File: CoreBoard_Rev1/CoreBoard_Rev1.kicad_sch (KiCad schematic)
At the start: 86 parts, among them J1 RJ45_LED_Shielded, SW1 SW_Push, SW10 SW_Push, SW11 SW_Push, SW12 SW_Push, SW13 SW_Push, SW14 SW_Push, SW15 SW_Push, SW16 SW_SPDT, SW2 SW_Push, SW3 SW_Push, SW4 SW_Push, SW5 SW_Push, SW6 SW_Push, SW7 SW_Push, SW8 SW_Push, SW9 SW_Push, U1 Teensy4.1_DEV-16771, U2 TSR_1-2450, U4 74HC148, U5 74HC148, U6 74HC00, U7 OKI

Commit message: connected remaining components
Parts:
- U2: footprint Converter_DCDC:Converter_DCDC_TRACO_TSR-1_THT -> MRDT_Devices:SHHD003A0A-SRZ
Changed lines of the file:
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@@
       (effects (font (size 1.27 1.27)))
     )
-    (property "Footprint" "Converter_DCDC:Converter_DCDC_TRACO_TSR-1_THT" (at 124.46 44.45 0)
+    (property "Footprint" "MRDT_Devices:SHHD003A0A-SRZ" (at 124.46 44.45 0)
       (effects (font (size 1.27 1.27) italic) (justify left) hide)
     )

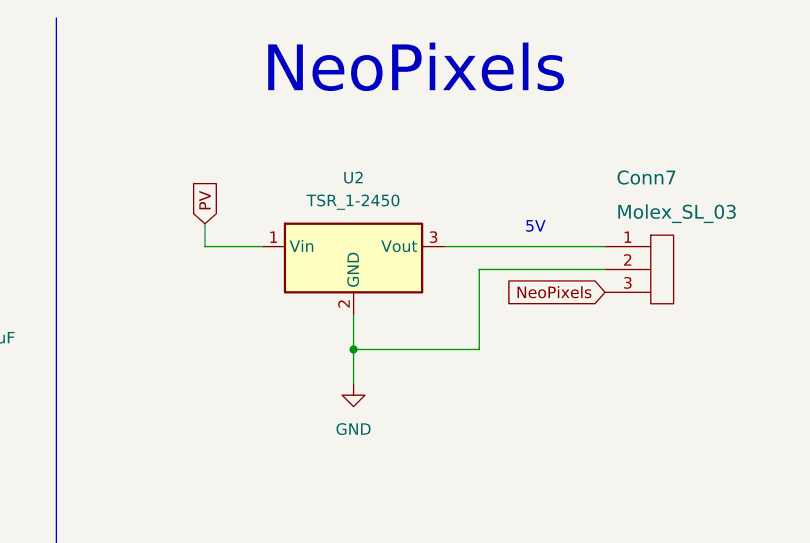
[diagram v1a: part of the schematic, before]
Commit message: updating button traces
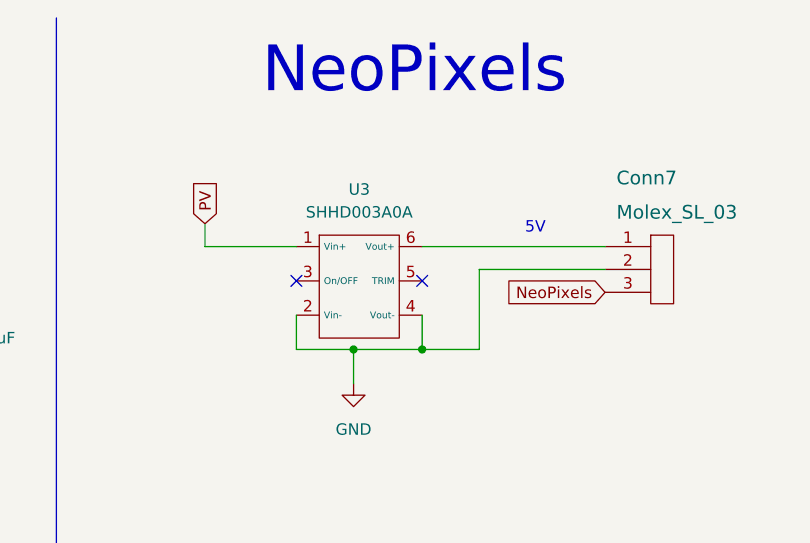
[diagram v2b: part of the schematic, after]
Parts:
- removed U2: TSR_1-2450, MRDT_Devices:SHHD003A0A-SRZ, symbol Regulator_Switching:TSR_1-2450
- added U3: SHHD003A0A, MRDT_Devices:SHHD003A0A-SRZ, symbol MRDT_Devices:SHHD003A0A
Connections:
- net GND: now also U3.2 (Vin-), U3.4 (Vout-)
- net PV: now also U3.1 (Vin+)
- net at Conn7.1: now also U3.6 (Vout+)
- no-connect marks 28 -> 30
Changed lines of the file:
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@@
   (junction (at 308.61 53.34) (diameter 0) (color 0 0 0 0)
   )
+  (junction (at 124.46 49.53) (diameter 0) (color 0 0 0 0)
+  )
   (junction (at 369.57 40.64) (diameter 0) (color 0 0 0 0)
   )
@@
   (junction (at 224.79 111.76) (diameter 0) (color 0 0 0 0)
   )
-  (junction (at 124.46 49.53) (diameter 0) (color 0 0 0 0)
+  (junction (at 132.08 49.53) (diameter 0) (color 0 0 0 0)
   )
   (junction (at 226.06 59.69) (diameter 0) (color 0 0 0 0)
@@
   (no_connect (at 144.78 182.88))
   (no_connect (at 53.34 193.04))
+  (no_connect (at 118.11 41.91))
   (no_connect (at 349.25 152.4))
   (no_connect (at 350.52 201.93))
@@
   (no_connect (at 53.34 223.52))
   (no_connect (at 93.98 256.54))
+  (no_connect (at 132.08 41.91))
   (no_connect (at 93.98 259.08))
   (no_connect (at 53.34 213.36))
@@
     (stroke (width 0) (type default))
   )
+  (wire (pts (xy 132.08 38.1) (xy 152.4 38.1))
+    (stroke (width 0) (type default))
+  )
   (wire (pts (xy 241.3 267.97) (xy 247.65 267.97))
     (stroke (width 0) (type default))
@@
     (stroke (width 0) (type default))
   )
+  (wire (pts (xy 132.08 45.72) (xy 132.08 49.53))
+    (stroke (width 0) (type default))
+  )
   (wire (pts (xy 373.38 144.78) (xy 373.38 179.07))
     (stroke (width 0) (type default))
@@
     (stroke (width 0) (type default))
   )
+  (wire (pts (xy 132.08 49.53) (xy 124.46 49.53))
+    (stroke (width 0) (type default))
+  )
   (wire (pts (xy 212.09 46.99) (xy 215.9 46.99))
     (stroke (width 0) (type default))
@@
     (stroke (width 0) (type default))
   )
-  (wire (pts (xy 107.95 38.1) (xy 114.3 38.1))
+  (wire (pts (xy 107.95 38.1) (xy 118.11 38.1))
     (stroke (width 0) (type default))
   )
@@
     (stroke (width 0) (type default))
   )
-  (wire (pts (xy 134.62 38.1) (xy 152.4 38.1))
-    (stroke (width 0) (type default))
-  )
   (wire (pts (xy 212.09 36.83) (xy 215.9 36.83))
     (stroke (width 0) (type default))
@@
     (stroke (width 0) (type default))
   )
+  (wire (pts (xy 118.11 49.53) (xy 124.46 49.53))
+    (stroke (width 0) (type default))
+  )
   (wire (pts (xy 236.22 49.53) (xy 236.22 59.69))
     (stroke (width 0) (type default))
@@
     (stroke (width 0) (type default))
   )
-  (wire (pts (xy 124.46 45.72) (xy 124.46 49.53))
-    (stroke (width 0) (type default))
-  )
   (wire (pts (xy 224.79 189.23) (xy 232.41 189.23))
     (stroke (width 0) (type default))
@@
     (stroke (width 0) (type default))
   )
+  (wire (pts (xy 118.11 45.72) (xy 118.11 49.53))
+    (stroke (width 0) (type default))
+  )
   (wire (pts (xy 212.09 44.45) (xy 215.9 44.45))
     (stroke (width 0) (type default))
@@
     (stroke (width 0) (type default))
   )
-  (wire (pts (xy 138.43 49.53) (xy 124.46 49.53))
+  (wire (pts (xy 138.43 49.53) (xy 132.08 49.53))
     (stroke (width 0) (type default))
   )
@@
     )
   )
+  (symbol (lib_id "MRDT_Devices:SHHD003A0A") (at 124.46 50.8 0) (unit 1)
+    (in_bom yes) (on_board yes) (dnp no) (fields_autoplaced)
+    (property "Reference" "U3" (at 125.095 31.75 0)
+      (effects (font (size 1.27 1.27)))
+    )
+    (property "Value" "SHHD003A0A" (at 125.095 34.29 0)
+      (effects (font (size 1.27 1.27)))
+    )
+    (property "Footprint" "MRDT_Devices:SHHD003A0A-SRZ" (at 124.46 50.8 0)
+      (effects (font (size 1.27 1.27)) hide)
+    )
+    (property "Datasheet" "https://www.digikey.com/en/products/detail/abb-power-conversion/SHHD003A0A41-SRZ/3993519" (at 124.46 50.8 0)
+      (effects (font (size 1.27 1.27)) hide)
+    )
+    (pin "1")
+    (pin "2")
+    (pin "3")
+    (pin "4")
+    (pin "5")
+    (pin "6")
+    (instances
+      (project "CoreBoard_Rev1"
+        (path "/33647808-cf2c-4b1c-bf2f-58fa6408b099"
+          (reference "U3") (unit 1)
+        )
+      )
+    )
+  )
   (symbol (lib_id "MRDT_Devices:OKI") (at 58.42 43.18 0) (unit 1)
     (in_bom yes) (on_board yes) (dnp no) (fields_autoplaced)
@@
         )
       )
-    )
-  )
-  (symbol (lib_id "Regulator_Switching:TSR_1-2450") (at 124.46 40.64 0) (unit 1)
-    (in_bom yes) (on_board yes) (dnp no) (fields_autoplaced)
-    (property "Reference" "U2" (at 124.46 30.48 0)
-      (effects (font (size 1.27 1.27)))
-    )
-    (property "Value" "TSR_1-2450" (at 124.46 33.02 0)
-      (effects (font (size 1.27 1.27)))
-    )
-    (property "Footprint" "MRDT_Devices:SHHD003A0A-SRZ" (at 124.46 44.45 0)
-      (effects (font (size 1.27 1.27) italic) (justify left) hide)
-    )
-    (property "Datasheet" "http://www.tracopower.com/products/tsr1.pdf" (at 124.46 40.64 0)
-      (effects (font (size 1.27 1.27)) hide)
-    )
-    (pin "1")
-    (pin "2")
-    (pin "3")
-    (instances
-      (project "CoreBoard_Rev1"
-        (path "/33647808-cf2c-4b1c-bf2f-58fa6408b099"
-          (reference "U2") (unit 1)
-        )
-      )

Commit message: Layout Changes
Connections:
- net GND: now also U3.3 (On/OFF)
- no-connect marks 30 -> 29
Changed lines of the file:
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@@
   (junction (at 260.35 147.32) (diameter 0) (color 0 0 0 0)
   )
+  (junction (at 134.62 49.53) (diameter 0) (color 0 0 0 0)
+  )
   (junction (at 283.21 259.08) (diameter 0) (color 0 0 0 0)
   )
@@
   (junction (at 212.09 259.08) (diameter 0) (color 0 0 0 0)
   )
+  (junction (at 115.57 45.72) (diameter 0) (color 0 0 0 0)
+  )
   (junction (at 224.79 111.76) (diameter 0) (color 0 0 0 0)
-  )
-  (junction (at 132.08 49.53) (diameter 0) (color 0 0 0 0)
   )
   (junction (at 226.06 59.69) (diameter 0) (color 0 0 0 0)
@@
   (no_connect (at 93.98 200.66))
   (no_connect (at 144.78 182.88))
+  (no_connect (at 132.08 41.91))
   (no_connect (at 53.34 193.04))
-  (no_connect (at 118.11 41.91))
   (no_connect (at 349.25 152.4))
   (no_connect (at 350.52 201.93))
@@
   (no_connect (at 53.34 223.52))
   (no_connect (at 93.98 256.54))
-  (no_connect (at 132.08 41.91))
   (no_connect (at 93.98 259.08))
   (no_connect (at 53.34 213.36))
@@
     (stroke (width 0) (type default))
   )
+  (wire (pts (xy 115.57 45.72) (xy 118.11 45.72))
+    (stroke (width 0) (type default))
+  )
   (wire (pts (xy 132.08 38.1) (xy 152.4 38.1))
     (stroke (width 0) (type default))
@@
     (stroke (width 0) (type default))
   )
-  (wire (pts (xy 132.08 45.72) (xy 132.08 49.53))
+  (wire (pts (xy 134.62 45.72) (xy 134.62 49.53))
     (stroke (width 0) (type default))
   )
@@
     (stroke (width 0) (type default))
   )
-  (wire (pts (xy 132.08 49.53) (xy 124.46 49.53))
+  (wire (pts (xy 124.46 49.53) (xy 134.62 49.53))
     (stroke (width 0) (type default))
   )
@@
     (stroke (width 0) (type default))
   )
+  (wire (pts (xy 115.57 41.91) (xy 115.57 45.72))
+    (stroke (width 0) (type default))
+  )
   (wire (pts (xy 281.94 181.61) (xy 283.21 181.61))
     (stroke (width 0) (type default))
@@
     (stroke (width 0) (type default))
   )
+  (wire (pts (xy 134.62 45.72) (xy 132.08 45.72))
+    (stroke (width 0) (type default))
+  )
   (wire (pts (xy 224.79 111.76) (xy 224.79 119.38))
     (stroke (width 0) (type default))
@@
     (stroke (width 0) (type default))
   )
+  (wire (pts (xy 118.11 41.91) (xy 115.57 41.91))
+    (stroke (width 0) (type default))
+  )
   (wire (pts (xy 260.35 259.08) (xy 267.97 259.08))
     (stroke (width 0) (type default))
@@
     (stroke (width 0) (type default))
   )
-  (wire (pts (xy 118.11 49.53) (xy 124.46 49.53))
+  (wire (pts (xy 115.57 49.53) (xy 124.46 49.53))
     (stroke (width 0) (type default))
   )
@@
     (stroke (width 0) (type default))
   )
-  (wire (pts (xy 118.11 45.72) (xy 118.11 49.53))
+  (wire (pts (xy 115.57 45.72) (xy 115.57 49.53))
     (stroke (width 0) (type default))
   )
@@
     (stroke (width 0) (type default))
   )
-  (wire (pts (xy 138.43 49.53) (xy 132.08 49.53))
-    (stroke (width 0) (type default))
-  )
+  (wire (pts (xy 138.43 49.53) (xy 134.62 49.53))
+    (stroke (width 0) (type default))
+  )

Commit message: Gerbs Generated
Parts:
- C2: footprint Capacitor_SMD:C_0603_1608Metric_Pad1.08x0.95mm_HandSolder -> Capacitor_SMD:C_1206_3216Metric_Pad1.33x1.80mm_HandSolder
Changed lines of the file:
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@@
       (effects (font (size 1.27 1.27)) (justify left))
     )
-    (property "Footprint" "Capacitor_SMD:C_0603_1608Metric_Pad1.08x0.95mm_HandSolder" (at 49.2252 50.8 0)
+    (property "Footprint" "Capacitor_SMD:C_1206_3216Metric_Pad1.33x1.80mm_HandSolder" (at 49.2252 50.8 0)
       (effects (font (size 1.27 1.27)) hide)
     )
